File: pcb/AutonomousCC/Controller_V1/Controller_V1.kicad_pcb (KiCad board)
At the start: 2 copper layers, 142.9 x 87.6 mm, 18 parts, among them J1 Antenna_Conn_02x04_Odd_Even, J2 USB1130-15-A_REVA, SW1 SW_12mm_Push, SW2 SW_12mm_Push, U1 COM-09032, U2 Pico, U3 COM-09032

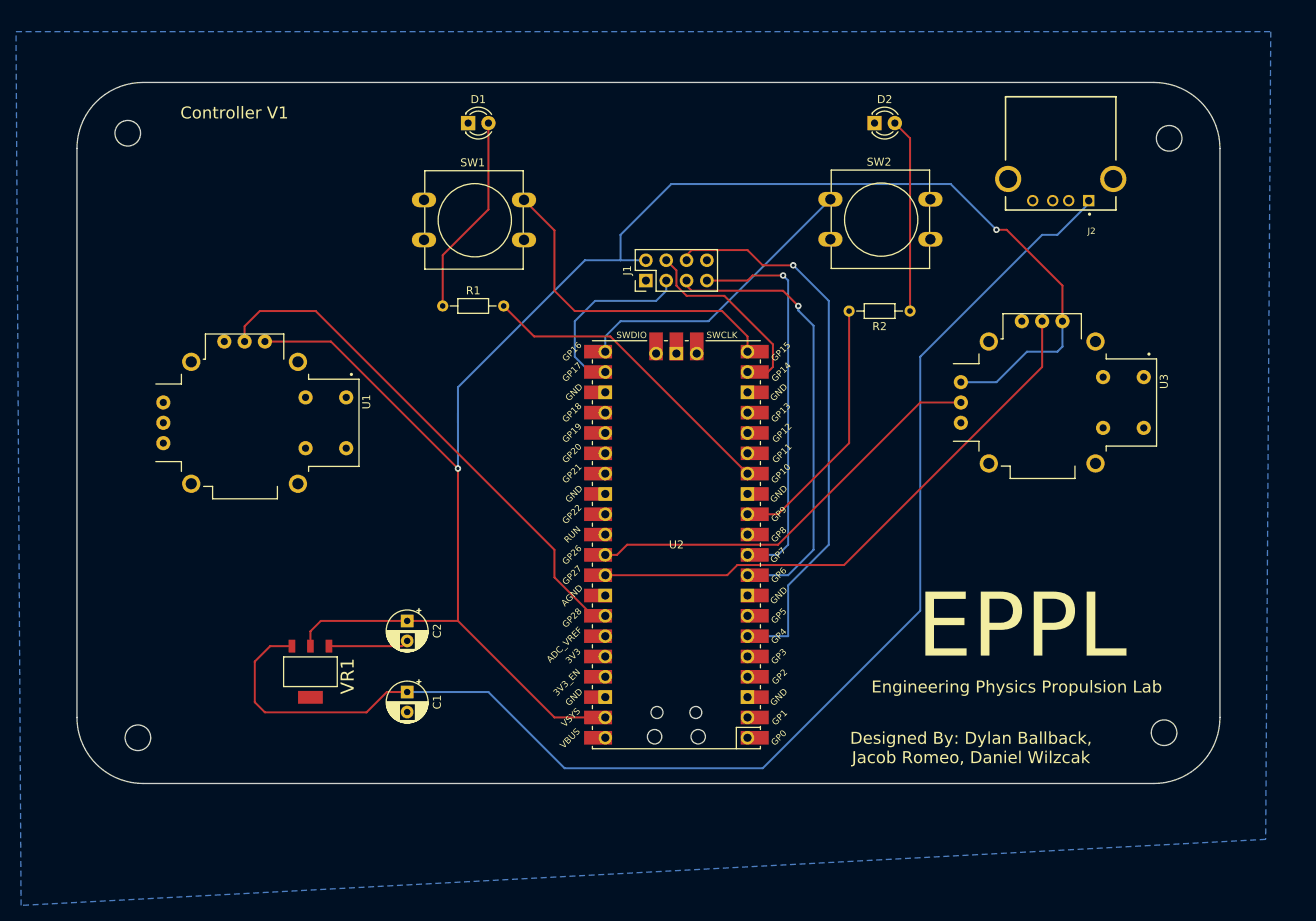
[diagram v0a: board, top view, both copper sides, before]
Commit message: Update Controller Antenna Pins
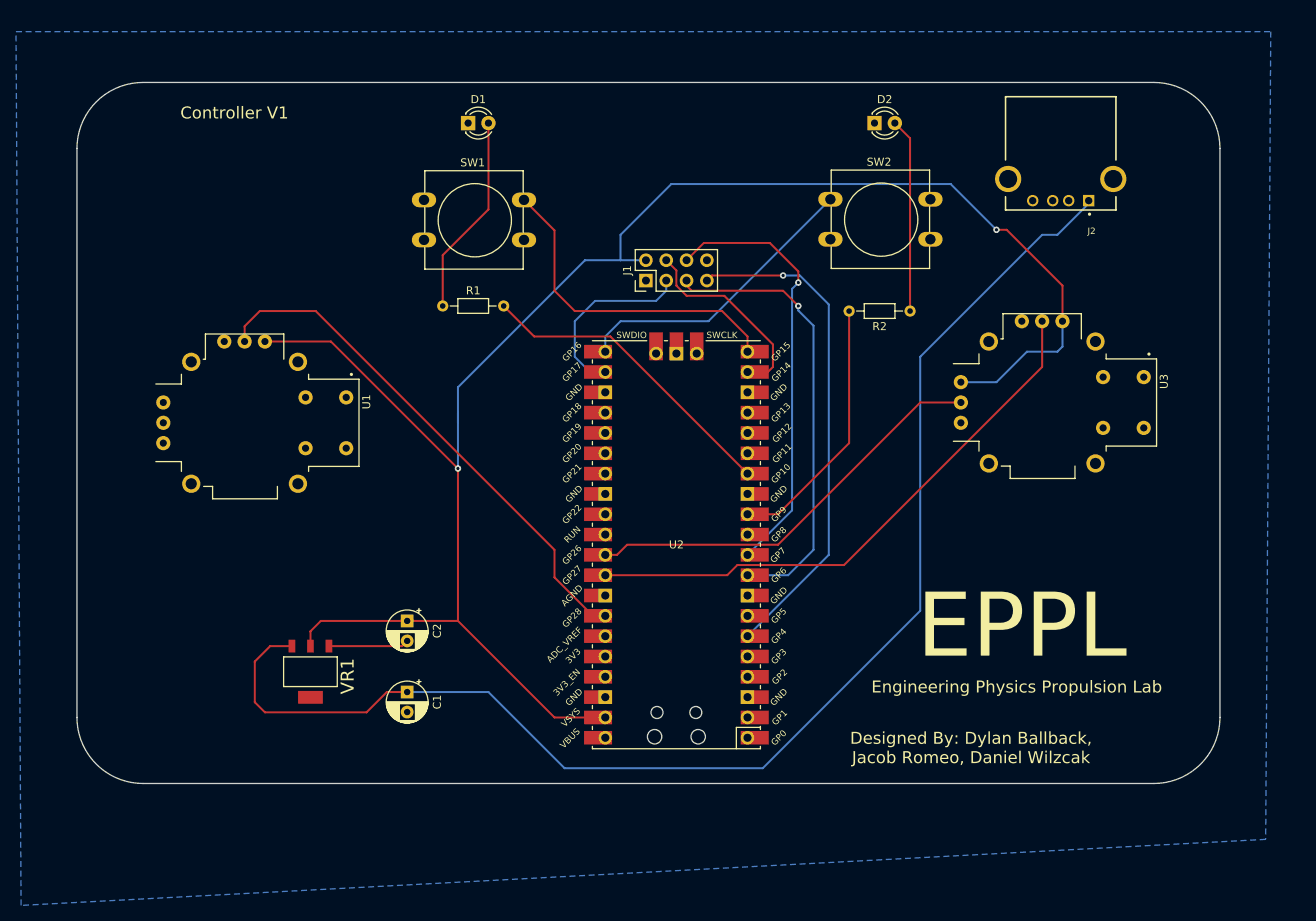
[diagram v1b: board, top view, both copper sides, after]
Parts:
- removed REF** (x4): MountingHole_3.2mm_M3, MountingHole:MountingHole_3.2mm_M3
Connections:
- J1 pad 6: GP04 -> GP07
- J1 pad 7: GP07 -> GP04
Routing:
- net GP04: track 70.4 -> 62.7 mm
- net GP07: track 49.3 -> 55.0 mm

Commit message: CC Controller and Brain VERSION 1.1
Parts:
- added H4: MountingHole, MountingHole:MountingHole_2.2mm_M2_Pad, F.Cu at (106.2, 132.9)
- added He: MountingHole, MountingHole:MountingHole_2.2mm_M2_Pad, F.Cu at (236.3, 132.9)
- added He: MountingHole, MountingHole:MountingHole_2.2mm_M2_Pad, F.Cu at (236.3, 57.7)
- added e: MountingHole, MountingHole:MountingHole_2.2mm_M2_Pad, F.Cu at (106.1, 57.5)
- moved J2 2.01 mm to (220.7, 62.8)
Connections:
- C2 pad 1: +3V3 -> +3.3VA
- J1 pad 2: +3V3 -> +3.3VA
- SW1 pad 2: GND -> +3V3
- SW2 pad 2: GND -> +3V3
- U2 pad 36: Net-(U2-Pad36) -> +3V3
- U2 pad 39: +3V3 -> +3.3VA
- VR1 pad 2: +3V3 -> +3.3VA
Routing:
- net +3.3VA: track 0.00 -> 101.1 mm, vias 0 -> 1
- net +3V3: track 224.0 -> 218.5 mm
- net +5V: track 168.5 -> 167.7 mm
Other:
- board text added: "Controller V1.1"
- board text removed: "Controller V1"
